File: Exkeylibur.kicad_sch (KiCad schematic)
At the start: 50 parts, among them J1 TRRS, J2 TRRS, SW1 SW_Push, SW10 SW_Push, SW11 SW_Push, SW12 SW_Push, SW13 SW_Push, SW14 SW_Push, SW15 SW_Push, SW16 SW_Push, SW17 SW_Push, SW18 SW_Push, SW19 SW_Push, SW2 SW_Push, SW20 SW_Push, SW21 SW_Push, SW22 SW_Push, SW23 SW_Push, SW24 SW_Push, SW25 SW_Push, SW26 SW_Push, SW27 SW_Push, SW28 SW_Push, SW29 SW_Push, SW3 SW_Push, SW30 SW_Push, SW31 SW_Push, SW32 SW_Push, SW33 SW_Push, SW34 SW_Push, SW35 SW_Push, SW36 SW_Push, SW37 SW_Push, SW38 SW_Push, SW39 SW_Push, SW4 SW_Push, SW40 SW_Push, SW41 SW_Push, SW42 SW_Push, SW5 SW_Push, SW6 SW_Push, SW7 SW_Push, SW8 SW_Push, SW9 SW_Push, U1 Elite-C, U2 Elite-C

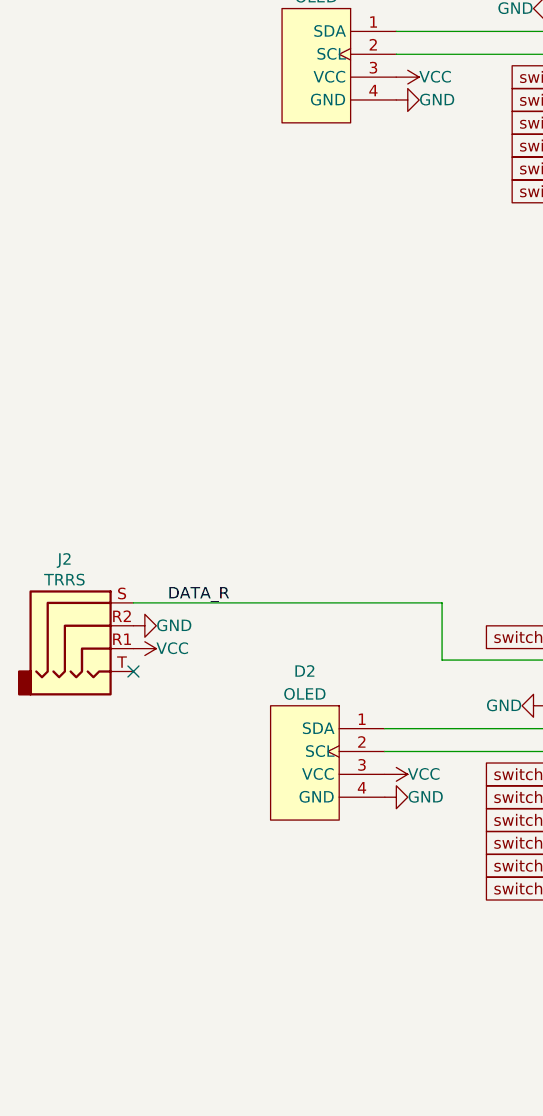
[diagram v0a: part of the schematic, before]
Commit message: add annotations for left and right
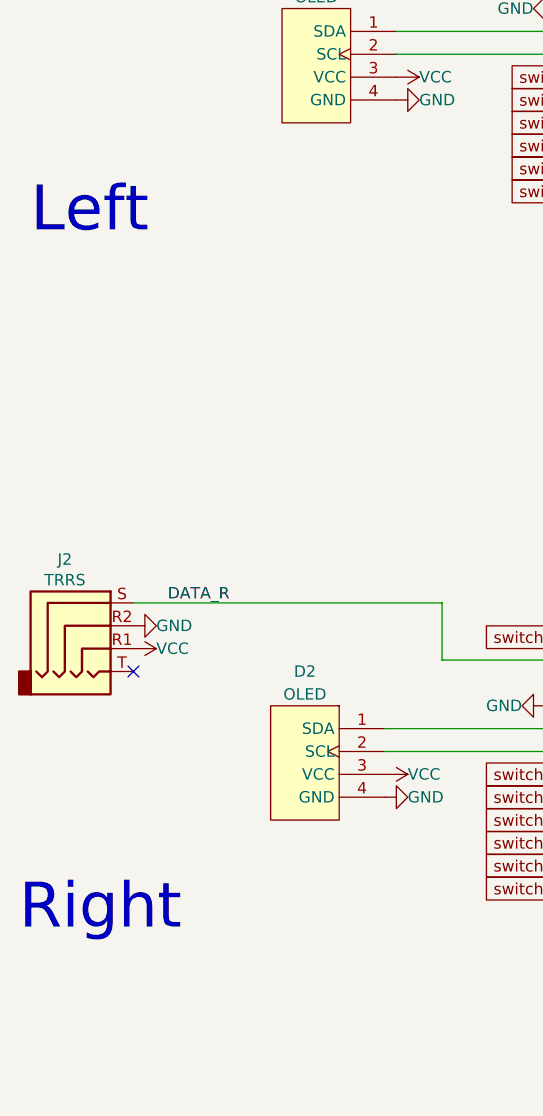
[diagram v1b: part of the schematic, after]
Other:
- note added: "Left"
- note added: "Right"
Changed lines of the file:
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@@
     (stroke (width 0) (type default) (color 0 0 0 0))
+  )
+  (text "Left" (at 41.91 57.15 0)
+    (effects (font (size 5 5)) (justify left bottom))
+  )
+  (text "Right" (at 40.64 134.62 0)
+    (effects (font (size 5 5)) (justify left bottom))
   )
   (label "RST" (at 152.4 29.21 0)

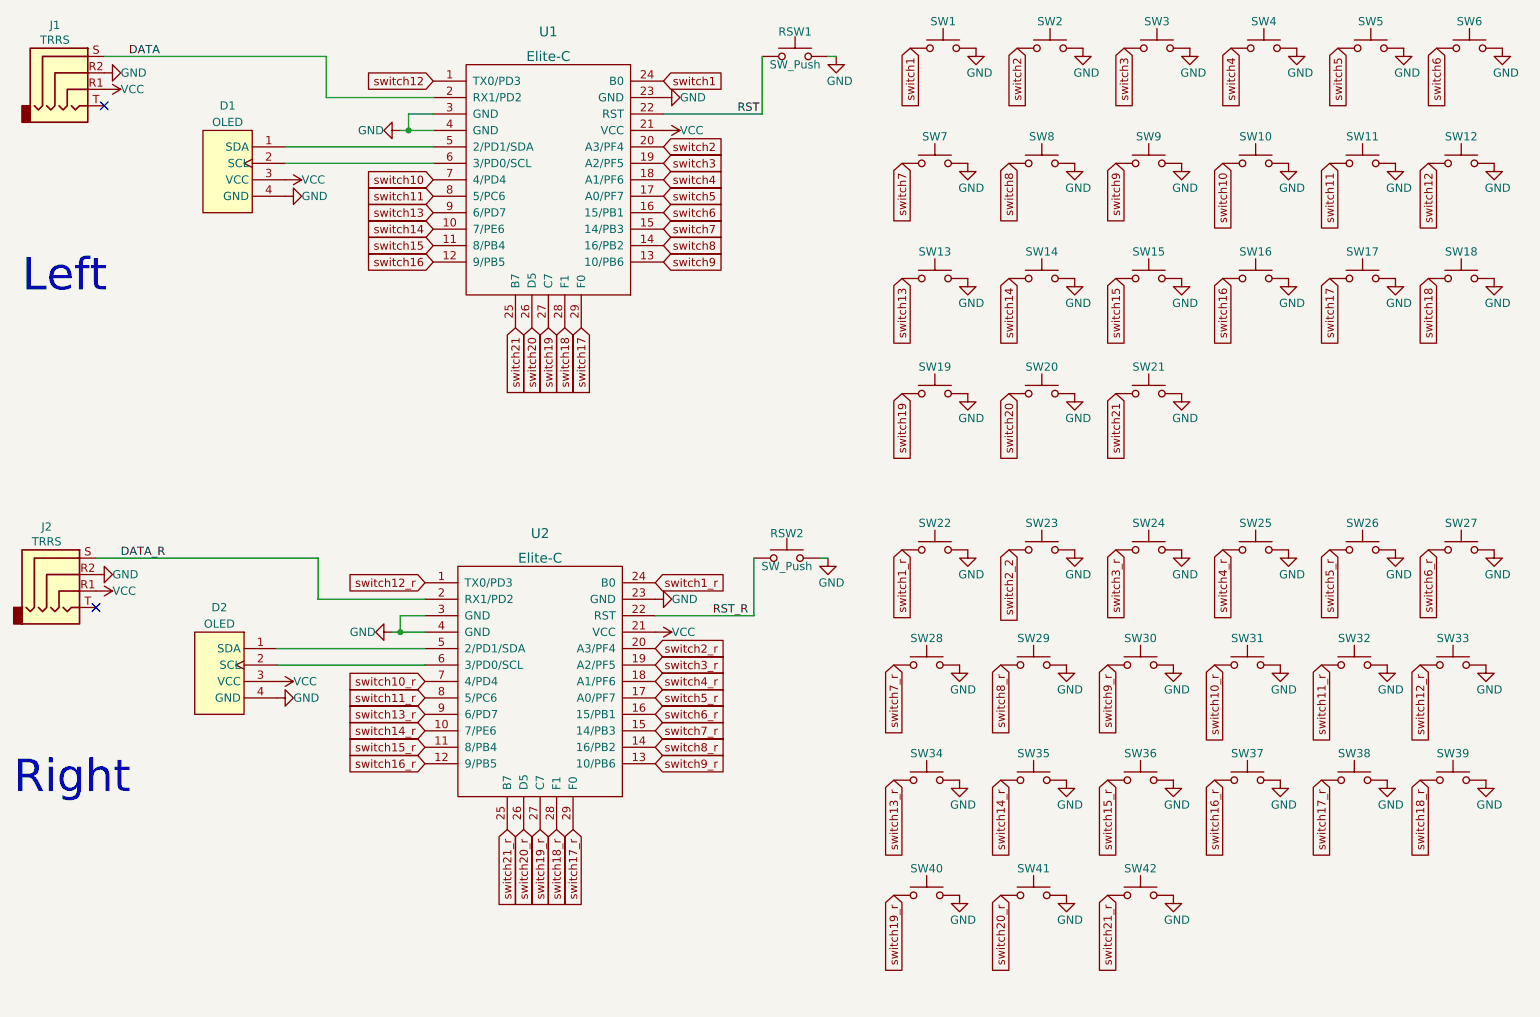
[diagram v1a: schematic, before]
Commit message: changes outlay to include 4 thumb keys
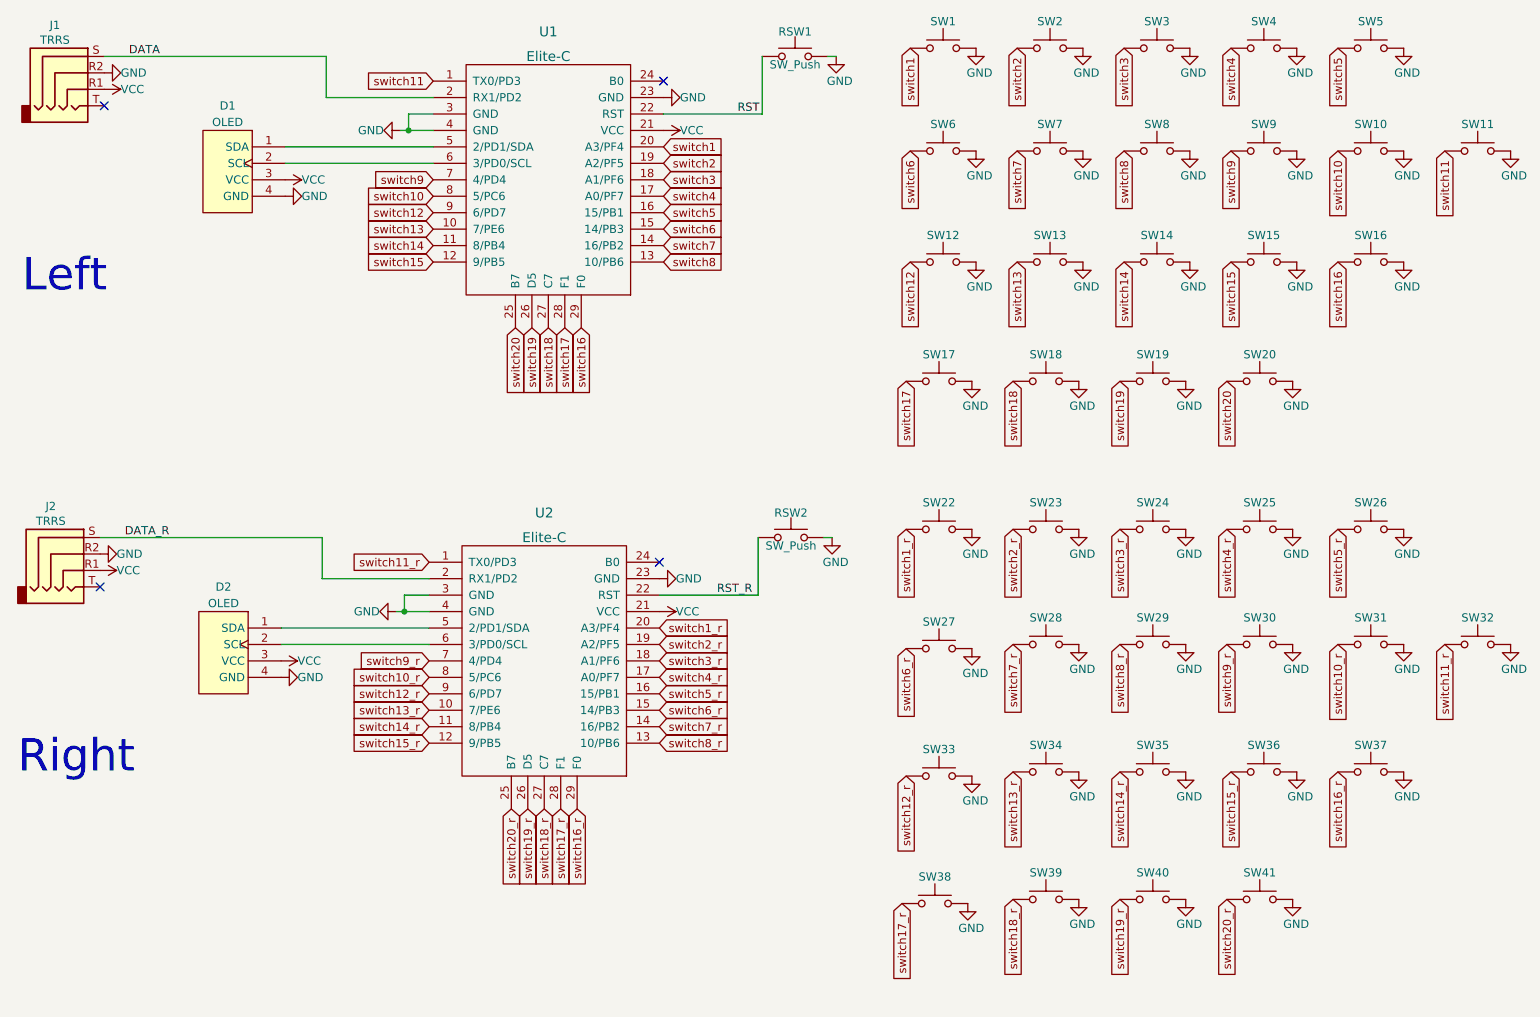
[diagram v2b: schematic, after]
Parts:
- removed SW21, SW42: SW_Push, symbol Switch:SW_Push
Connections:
- net switch21 is gone; now on net switch20: U1.25 (B7)
- net switch21_r is gone; now on net switch20_r: U2.25 (B7)
- net switch2_2 is gone; now on net switch2_r: SW23.1
- net switch1: now also U1.20 (A3/PF4); no longer U1.24 (B0)
- net switch10: now also U1.8 (5/PC6); no longer U1.7 (4/PD4)
- net switch10_r: now also U2.8 (5/PC6); no longer U2.7 (4/PD4)
- net switch11: now also U1.1 (TX0/PD3); no longer U1.8 (5/PC6)
- net switch11_r: now also U2.1 (TX0/PD3); no longer U2.8 (5/PC6)
- net switch12: now also U1.9 (6/PD7); no longer U1.1 (TX0/PD3)
- net switch12_r: now also U2.9 (6/PD7); no longer U2.1 (TX0/PD3)
- net switch13: now also U1.10 (7/PE6); no longer U1.9 (6/PD7)
- net switch13_r: now also U2.10 (7/PE6); no longer U2.9 (6/PD7)
- net switch14: now also U1.11 (8/PB4); no longer U1.10 (7/PE6)
- net switch14_r: now also U2.11 (8/PB4); no longer U2.10 (7/PE6)
- net switch15: now also U1.12 (9/PB5); no longer U1.11 (8/PB4)
- net switch15_r: now also U2.12 (9/PB5); no longer U2.11 (8/PB4)
- net switch16: now also U1.29 (F0); no longer U1.12 (9/PB5)
- net switch16_r: now also U2.29 (F0); no longer U2.12 (9/PB5)
- net switch17: now also U1.28 (F1); no longer U1.29 (F0)
- net switch17_r: now also U2.28 (F1); no longer U2.29 (F0)
- net switch18: now also U1.27 (C7); no longer U1.28 (F1)
- net switch18_r: now also U2.27 (C7); no longer U2.28 (F1)
- net switch19: now also U1.26 (D5); no longer U1.27 (C7)
- net switch19_r: now also U2.26 (D5); no longer U2.27 (C7)
- net switch1_r: now also U2.20 (A3/PF4); no longer U2.24 (B0)
- net switch2: now also U1.19 (A2/PF5); no longer U1.20 (A3/PF4)
- net switch20: no longer U1.26 (D5)
- net switch20_r: no longer U2.26 (D5)
- net switch2_r: now also U2.19 (A2/PF5); no longer U2.20 (A3/PF4)
- net switch3: now also U1.18 (A1/PF6); no longer U1.19 (A2/PF5)
- net switch3_r: now also U2.18 (A1/PF6); no longer U2.19 (A2/PF5)
- net switch4: now also U1.17 (A0/PF7); no longer U1.18 (A1/PF6)
- net switch4_r: now also U2.17 (A0/PF7); no longer U2.18 (A1/PF6)
- net switch5: now also U1.16 (15/PB1); no longer U1.17 (A0/PF7)
- net switch5_r: now also U2.16 (15/PB1); no longer U2.17 (A0/PF7)
- net switch6: now also U1.15 (14/PB3); no longer U1.16 (15/PB1)
- net switch6_r: now also U2.15 (14/PB3); no longer U2.16 (15/PB1)
- net switch7: now also U1.14 (16/PB2); no longer U1.15 (14/PB3)
- net switch7_r: now also U2.14 (16/PB2); no longer U2.15 (14/PB3)
- net switch8: now also U1.13 (10/PB6); no longer U1.14 (16/PB2)
- net switch8_r: now also U2.13 (10/PB6); no longer U2.14 (16/PB2)
- net switch9: now also U1.7 (4/PD4); no longer U1.13 (10/PB6)
- net switch9_r: now also U2.7 (4/PD4); no longer U2.13 (10/PB6)
- no-connect marks 2 -> 4
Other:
- moved on the sheet: D2, J2, RSW2, SW10, SW11, SW12, SW13, SW14, SW15, SW16, SW17, SW18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
